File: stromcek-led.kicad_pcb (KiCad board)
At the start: 2 copper layers, 89.6 x 124.4 mm, 21 parts, among them J1 Conn_01x05_Female, SW1 SW_Push

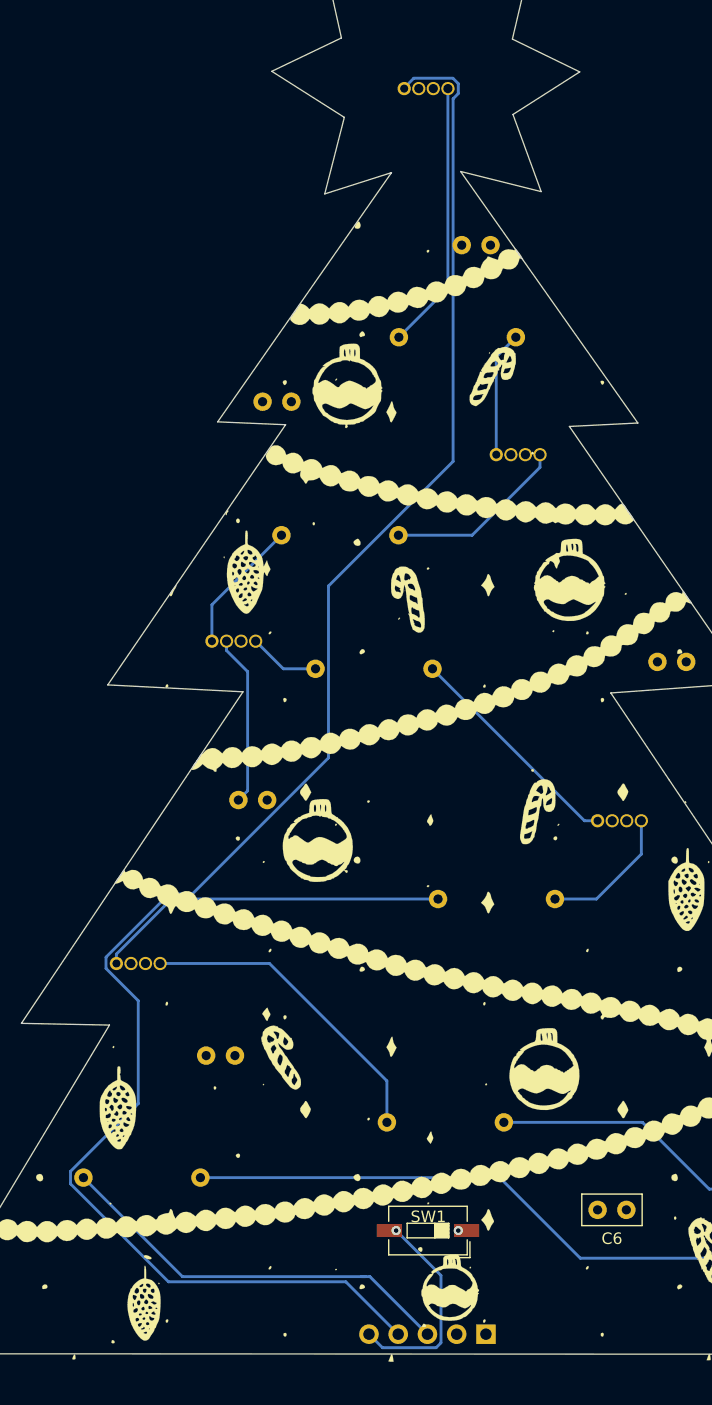
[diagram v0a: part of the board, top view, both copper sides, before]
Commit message: fixed D1 VCC, C1 crossing track, keepout on D1
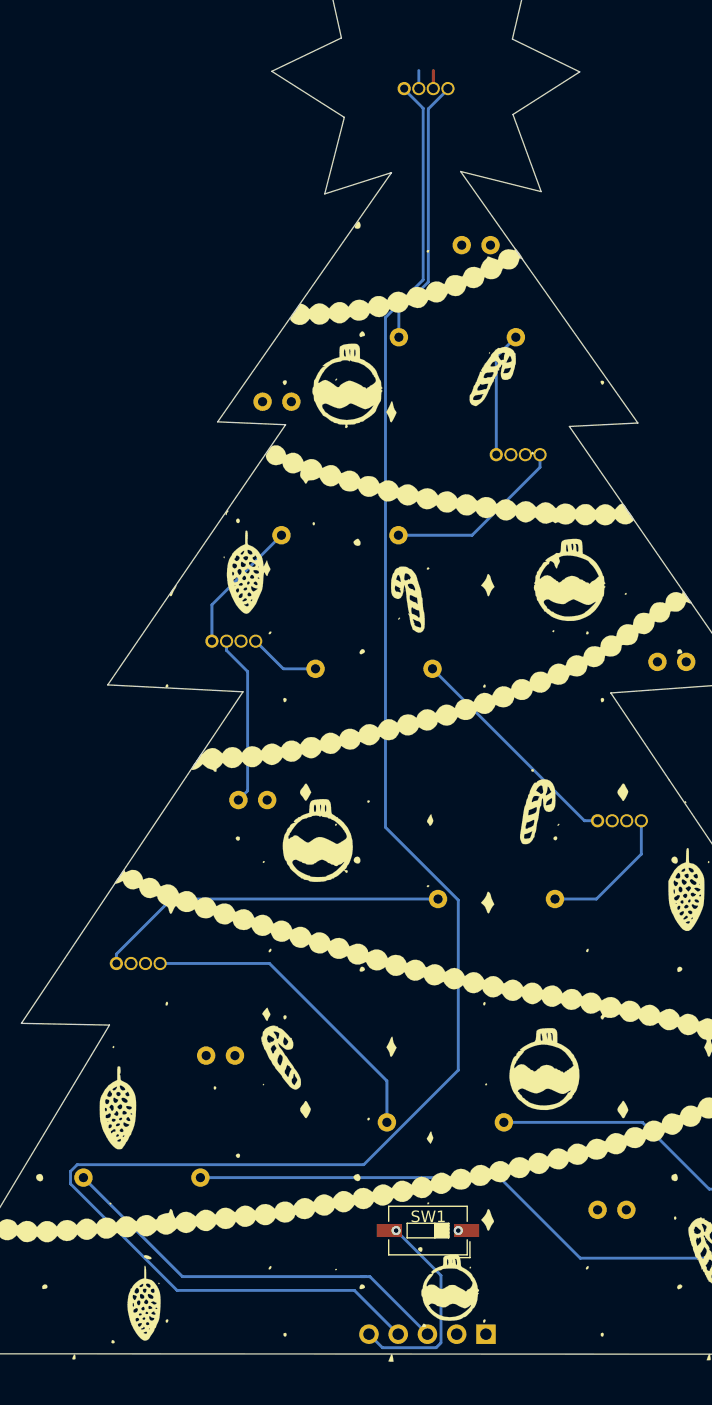
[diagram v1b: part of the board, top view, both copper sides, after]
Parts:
- C6: moved to B.Cu
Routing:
- net /DOUT: track 152.2 -> 162.2 mm
- net /VCC: track 14.9 -> 16.5 mm
- net /GND: track 0.00 -> 1.57 mm
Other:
- net class Default: clearance 0.2 -> 0.1
- rule trace_clearance: 0.2 -> 0.1
